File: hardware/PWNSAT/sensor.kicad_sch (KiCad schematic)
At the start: 15 parts, among them U1 ICM-42670-P, U2 SX1262IMLTRT, U4 BME280, U5 PE4259-63, Y3 CF4032M00010001

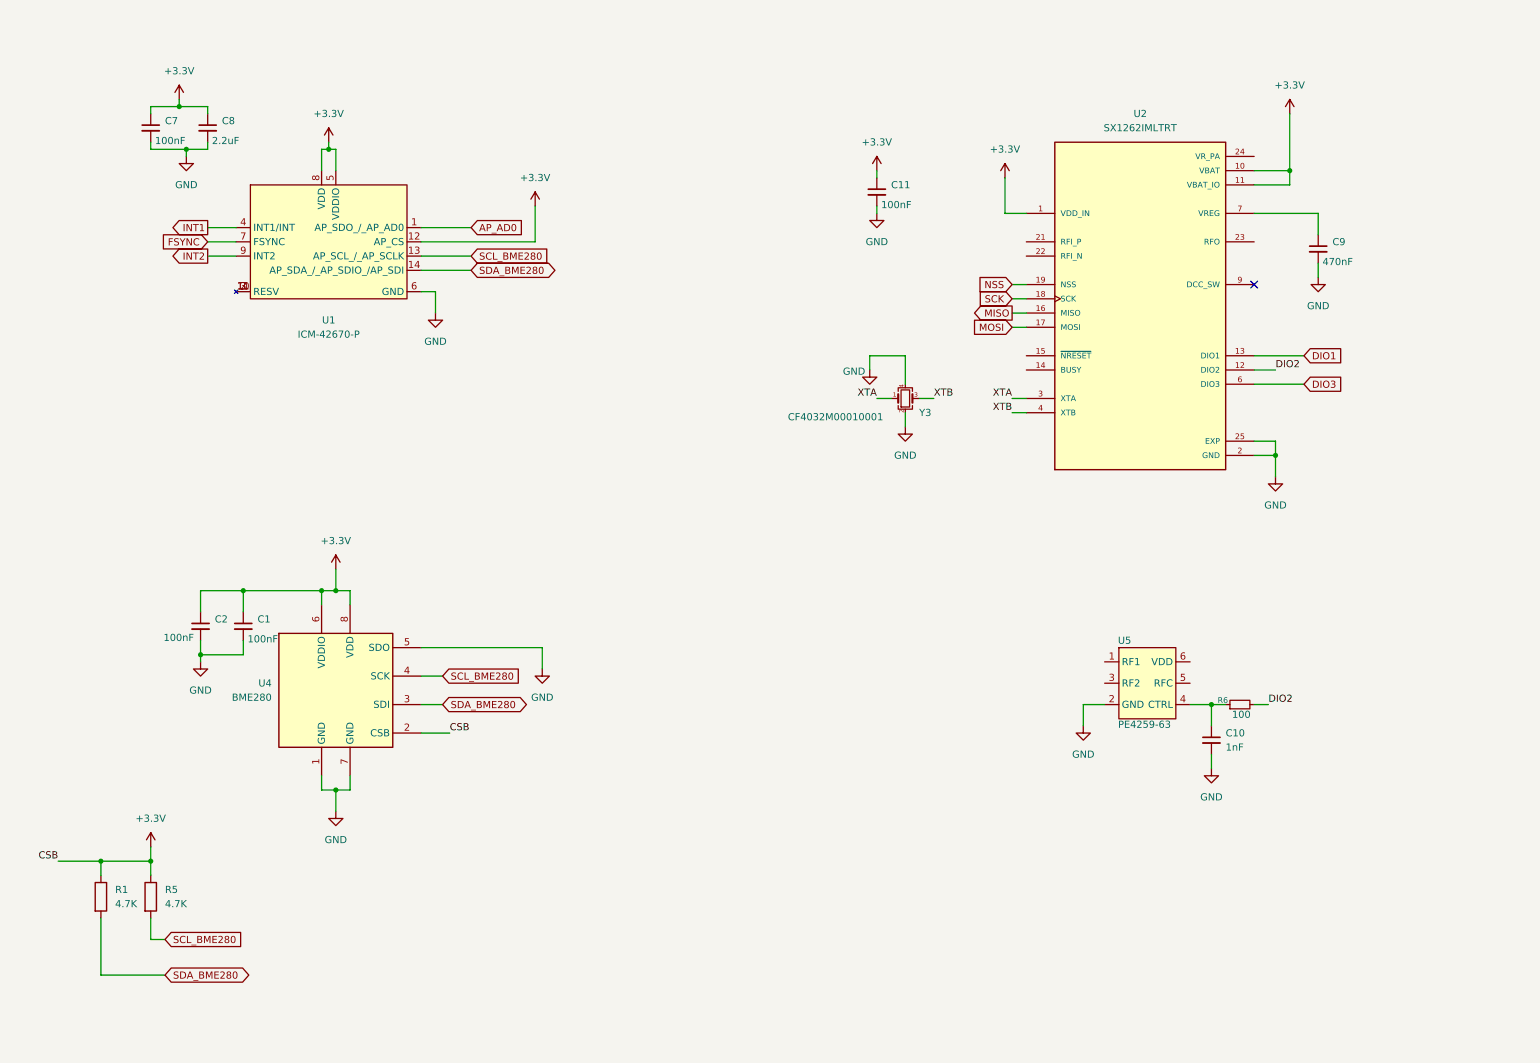
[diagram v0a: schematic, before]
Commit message: Feat(hw):Added_LoRa_module
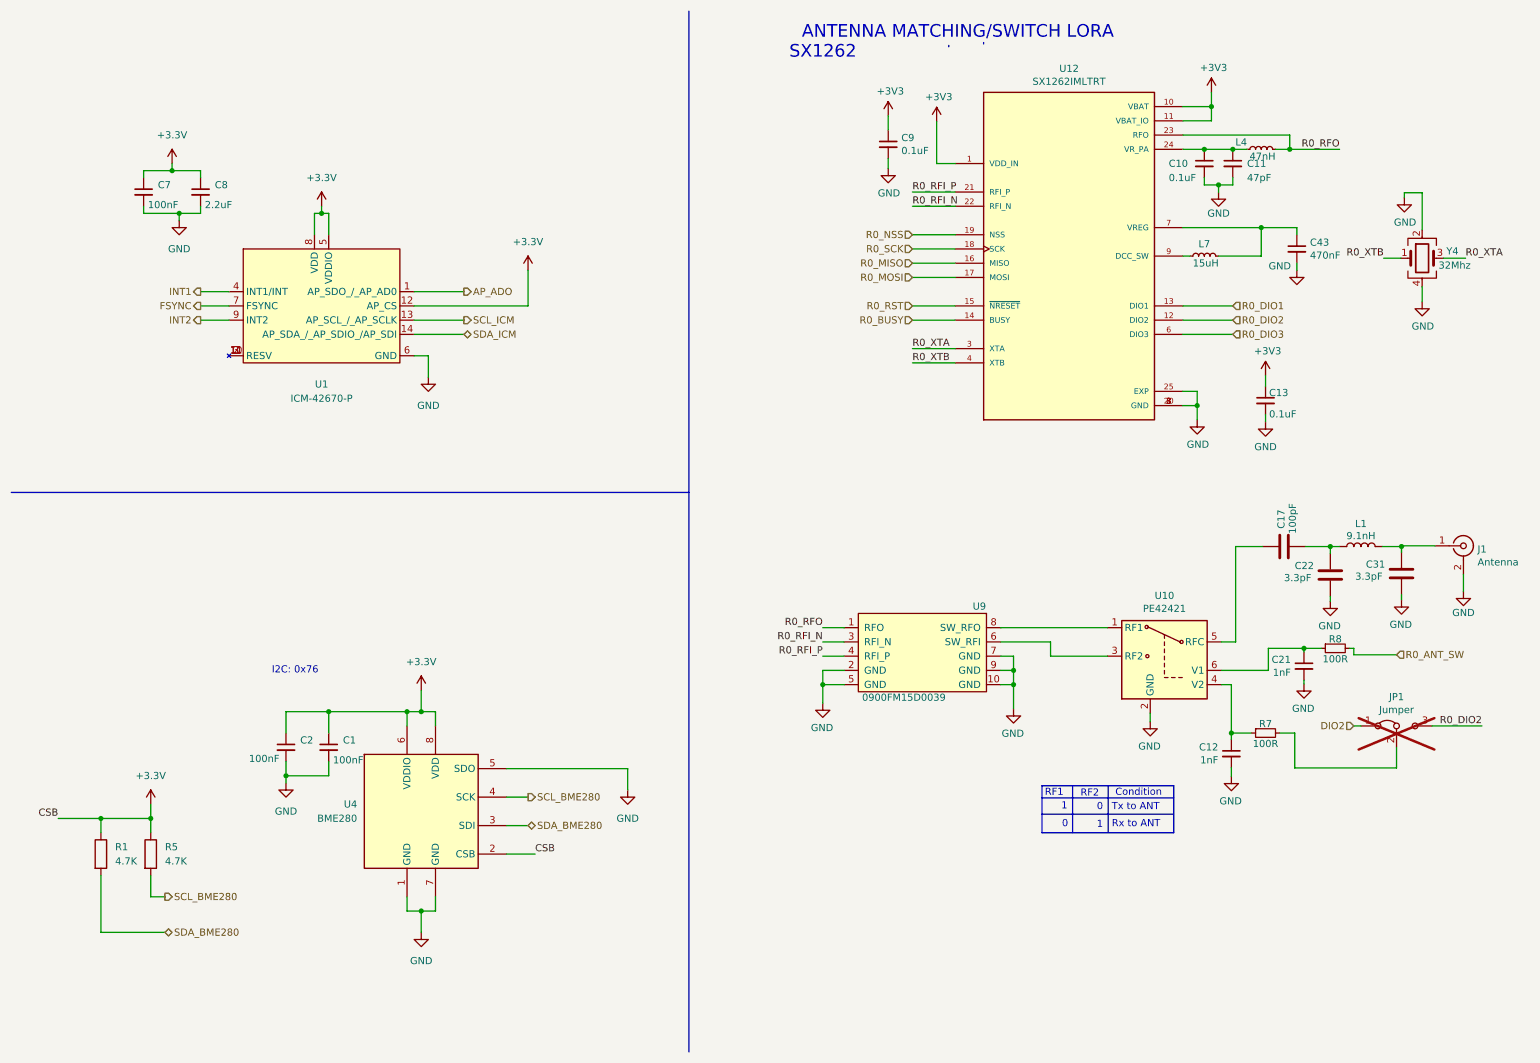
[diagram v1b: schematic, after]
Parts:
- removed C10: 1nF, symbol Device:C_Small
- removed C11: 100nF, symbol Device:C_Small
- removed C9: 470nF, symbol Device:C_Small
- removed R6: 100, symbol Device:R_Small
- removed U2: SX1262IMLTRT, SX1262IMLTRT:QFN50P400X400X100-25N, symbol SX1262IMLTRT:SX1262IMLTRT
- removed U5: PE4259-63, symbol Cubesat:PE4259-63
- removed Y3: CF4032M00010001, symbol Device:Crystal_GND24_Small
- added C10, C13, C9: 0.1uF, Capacitor_SMD:C_0402_1005Metric, symbol CatSniffer-rescue:C_Small-Device-CatStick-rescue-CatSniffer-rescue
- added C11: 47pF, Capacitor_SMD:C_0402_1005Metric, symbol CatSniffer-rescue:C_Small-Device-CatStick-rescue-CatSniffer-rescue
- added C12, C21: 1nF, Capacitor_SMD:C_0402_1005Metric, symbol CatSniffer-rescue:C_Small-Device-CatStick-rescue-CatSniffer-rescue
- added C17: 100pF, Capacitor_SMD:C_0402_1005Metric, symbol CatSniffer-rescue:C-Device-CatStick-rescue-CatSniffer-rescue
- added C22, C31: 3.3pF, Capacitor_SMD:C_0402_1005Metric, symbol CatSniffer-rescue:C-Device-CatStick-rescue-CatSniffer-rescue
- added C43: 470nF, Capacitor_SMD:C_0402_1005Metric, symbol CatSniffer-rescue:C_Small-Device-CatStick-rescue-CatSniffer-rescue
- added J1: Antenna, FlatSat:SMA_EDGE, symbol CatSniffer-rescue:Conn_Coaxial-Connector-CatStick-rescue-CatSniffer-rescue
- added JP1: Jumper, Jumper:SolderJumper-3_P1.3mm_Bridged12_RoundedPad1.0x1.5mm_NumberLabels, symbol CatSniffer-rescue:Jumper_3_Bridged12-Jumper-CatStick-rescue-CatSniffer-rescue
- added L1: 9.1nH, Inductor_SMD:L_0603_1608Metric, symbol CatSniffer-rescue:L-Device-CatStick-rescue-CatSniffer-rescue
- added L4: 47nH, Inductor_SMD:L_0603_1608Metric, symbol CatSniffer-rescue:L_Small-Device-CatStick-rescue-CatSniffer-rescue
- added L7: 15uH, Inductor_SMD:L_0603_1608Metric, symbol CatSniffer-rescue:L_Small-Device-CatStick-rescue-CatSniffer-rescue
- added R7, R8: 100R, Resistor_SMD:R_0402_1005Metric, symbol CatSniffer-rescue:R_Small-Device-CatStick-rescue-CatSniffer-rescue
- added U10: PE42421, Package_TO_SOT_SMD:SOT-363_SC-70-6, symbol CatSniffer-rescue:MASWSS0115-RF_Switch-CatStick-rescue-CatSniffer-rescue
- added U12: SX1262IMLTRT, Package_DFN_QFN:QFN-24-1EP_4x4mm_P0.5mm_EP2.65x2.65mm, symbol SX1262IMLTRT:SX1262IMLTRT
- added U9: 0900FM15D0039, FlatSat:0900FM15D0039E, symbol CatSniffer-rescue:0900FM15D0039-Electronic_Cats-CatStick-rescue-CatSniffer-resc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
- added Y4: 32Mhz, Crystal:Crystal_SMD_2520-4Pin_2.5x2.0mm, symbol CatSniffer-rescue:Crystal_GND24-Device-CatStick-rescue-CatSniffer-rescue
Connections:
- net DIO2: now also JP1.1 (A)
- net GND: now also C10.2, C11.2, C12.2, C13.2, C21.2, C22.2, C31.2, C43.2, C9.2, J1.2 (Ext), U10.2 (GND), U12.2 (GND), U12.20 (GND), U12.25 (EXP), U12.5 (GND), U12.8 (GND), U9.10 (GND), U9.2 (GND), U9.5 (GND), U9.7 (GND), U9.9 (GND), Y4.2, Y4.4
- net SCL_BME280: no longer U1.13 (AP_SCL_/_AP_SCLK)
- net SDA_BME280: no longer U1.14 (AP_SDA_/_AP_SDIO_/AP_SDI)
- net AP_AD0 renamed AP_ADO
- new net: C31.1, J1.1 (In), L1.1
- new net: C17.2, C22.1, L1.2
- new net: JP1.2 (C), R7.2
- new net: C12.1, R7.1, U10.4 (V2)
- new net: U10.1 (RF1), U9.8 (SW_RFO)
- new net: U10.3 (RF2), U9.6 (SW_RFI)
- new net: C17.1, U10.5 (RFC)
- new net: C21.1, R8.1, U10.6 (V1)
- new net: L7.1, U12.9 (DCC_SW)
- new net: C43.1, L7.2, U12.7 (VREG)
- new net: C10.1, C11.1, L4.1, U12.24 (VR_PA)
- new net +3V3: C13.1, C9.1, U12.1 (VDD_IN), U12.10 (VBAT), U12.11 (VBAT_IO)
- new net R0_ANT_SW: R8.2
- new net R0_BUSY: U12.14 (BUSY)
- new net R0_DIO1: U12.13 (DIO1)
- new net R0_DIO2: JP1.3 (B), U12.12 (DIO2)
- new net R0_DIO3: U12.6 (DIO3)
- new net R0_MISO: U12.16 (MISO)
- new net R0_MOSI: U12.17 (MOSI)
- new net R0_NSS: U12.19 (NSS)
- new net R0_RFI_N: U12.22 (RFI_N), U9.3 (RFI_N)
- new net R0_RFI_P: U12.21 (RFI_P), U9.4 (RFI_P)
- new net R0_RFO: L4.2, U12.23 (RFO), U9.1 (RFO)
- new net R0_RST: U12.15 (~{NRESET})
- new net R0_SCK: U12.18 (SCK)
- new net R0_XTA: U12.3 (XTA), Y4.3
- new net R0_XTB: U12.4 (XTB), Y4.1
- new net SCL_ICM: U1.13 (AP_SCL_/_AP_SCLK)
- new net SDA_ICM: U1.14 (AP_SDA_/_AP_SDIO_/AP_SDI)
- no-connect marks 1 -> 0
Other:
- note added: "0"
- note added: "1"
- note added: "ANTENNA MATCHING/SWITCH LORA"
- note added: "Condition"
- note added: "I2C: 0x76"
- note added: "RF1"
- note added: "RF2"
- note added: "Rx to ANT"
- note added: "SX1262"
- note added: "Tx to ANT"
- moved on the sheet: C1, C2, C7, C8, R1, R5, U1, U4

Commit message: feat(Hw): Added_BOM
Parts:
- C1, C2, C7: footprint (none) -> Capacitor_SMD:C_0402_1005Metric; #LCSC (none) -> C56392; LCSC# (none) -> C56392
- C10, C13, C9: #LCSC (none) -> C56392
- C11: #LCSC (none) -> C437519
- C12, C21: #LCSC (none) -> C710873
- C17: #LCSC (none) -> C541374
- C22, C31: #LCSC (none) -> C1565
- C43: #LCSC (none) -> C47339
- J1: #LCSC (none) -> C530661
- JP1: LCSC# (none) -> ---
- L1: #LCSC (none) -> C395094
- L4: #LCSC (none) -> C578001
- L7: #LCSC (none) -> C57838
- R1, R5: footprint (none) -> Resistor_SMD:R_0402_1005Metric_Pad0.72x0.64mm_HandSolder; #LCSC (none) -> C400631; LCSC# (none) -> C400631
- R7, R8: #LCSC (none) -> C25076
- U1: #LCSC (none) -> C3288646
- U10: #LCSC (none) -> C470893
- U12: #LCSC (none) -> C191341
- U4: #LCSC (none) -> C92489
- U9: MANUFACTURER (none) -> 0900FM15D0039E
- Y4: #LCSC (none) -> C255969
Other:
- note added: "ICM-42670-P"

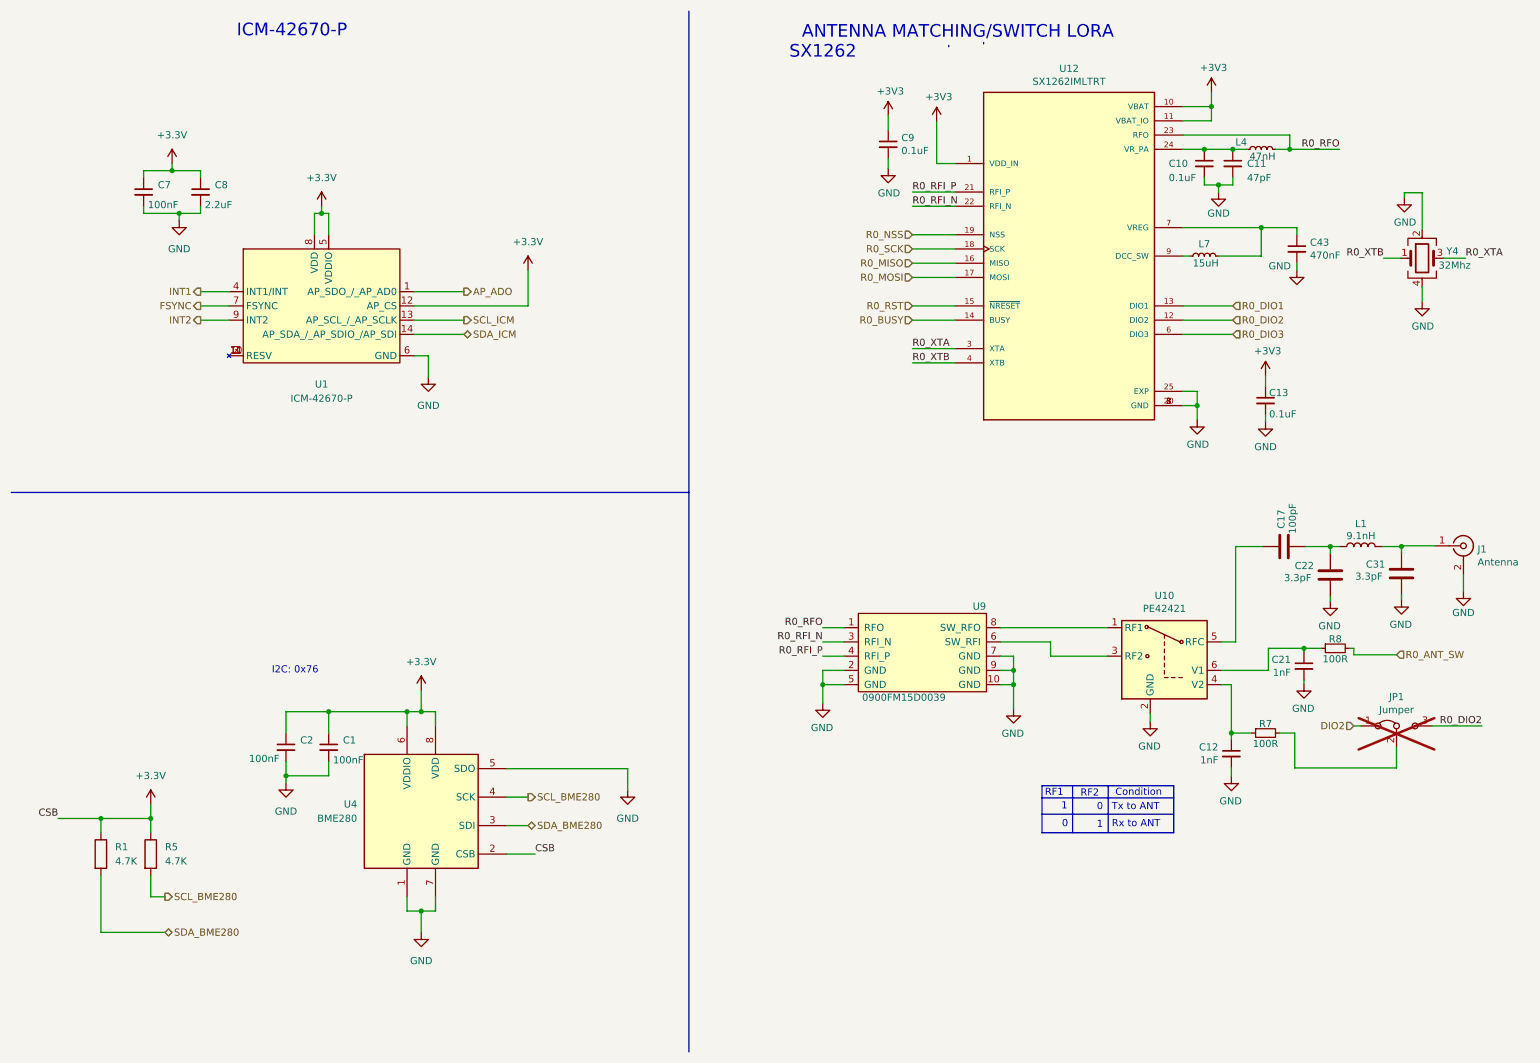
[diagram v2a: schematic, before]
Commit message: feat(Hw):Sch_Updated
Pending_Sensor_Connector
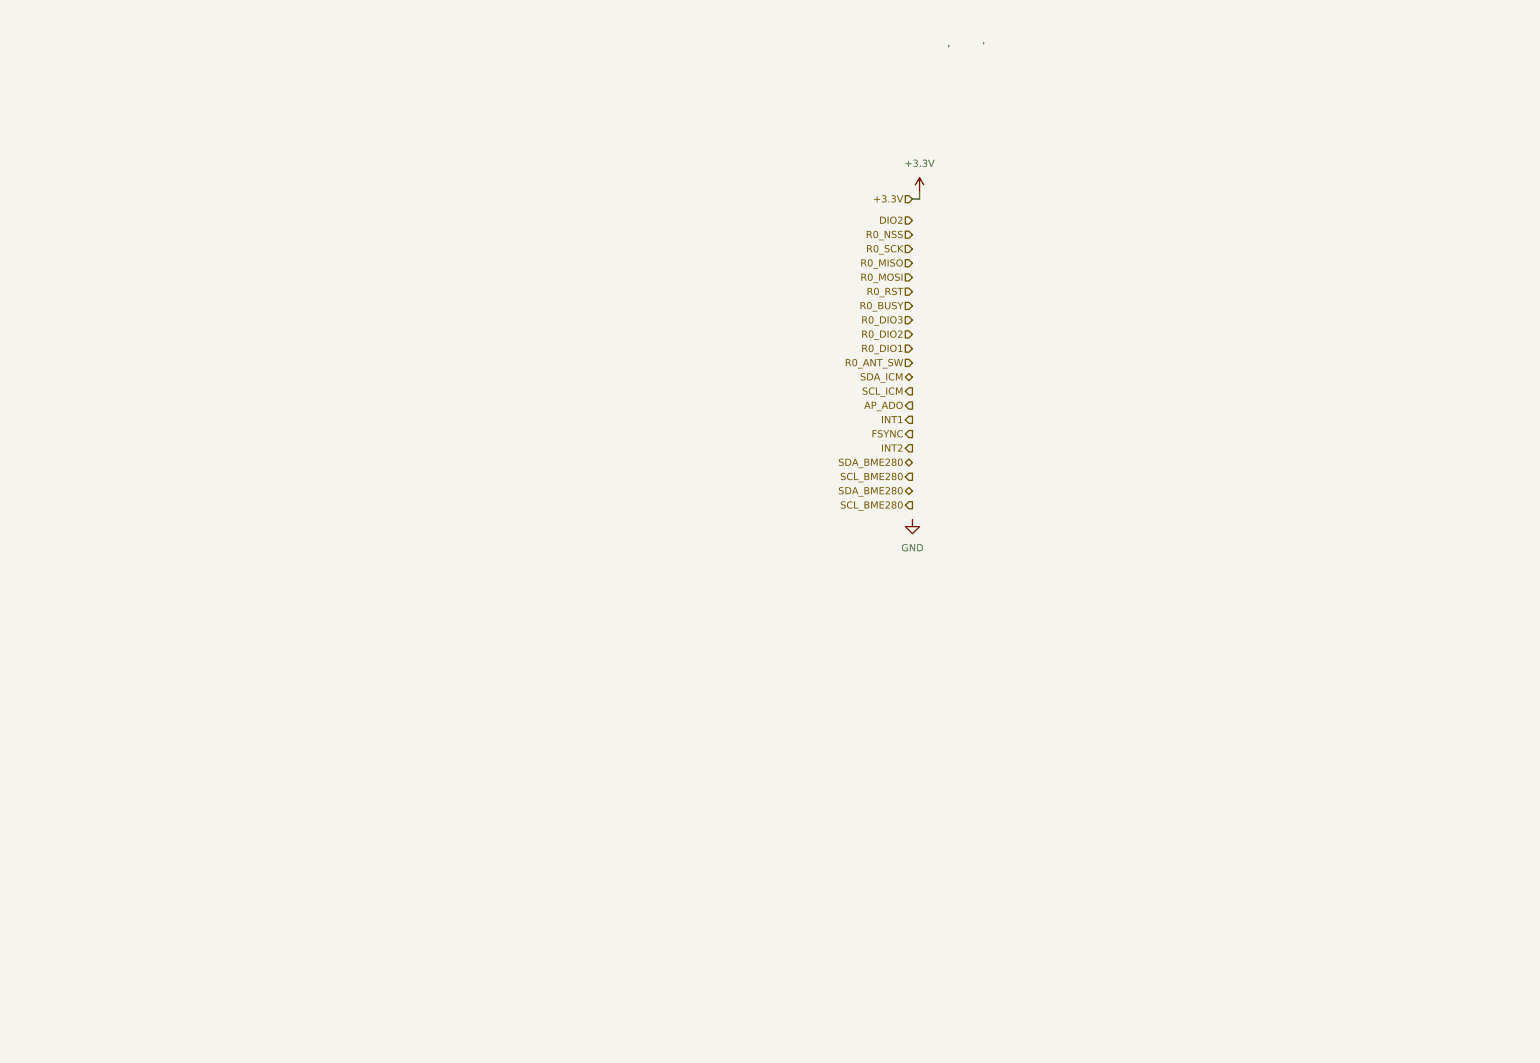
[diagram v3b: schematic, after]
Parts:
- removed C1, C2, C7: 100nF, Capacitor_SMD:C_0402_1005Metric, symbol Device:C_Small
- removed C10, C13, C9: 0.1uF, Capacitor_SMD:C_0402_1005Metric, symbol CatSniffer-rescue:C_Small-Device-CatStick-rescue-CatSniffer-rescue
- removed C11: 47pF, Capacitor_SMD:C_0402_1005Metric, symbol CatSniffer-rescue:C_Small-Device-CatStick-rescue-CatSniffer-rescue
- removed C12, C21: 1nF, Capacitor_SMD:C_0402_1005Metric, symbol CatSniffer-rescue:C_Small-Device-CatStick-rescue-CatSniffer-rescue
- removed C17: 100pF, Capacitor_SMD:C_0402_1005Metric, symbol CatSniffer-rescue:C-Device-CatStick-rescue-CatSniffer-rescue
- removed C22, C31: 3.3pF, Capacitor_SMD:C_0402_1005Metric, symbol CatSniffer-rescue:C-Device-CatStick-rescue-CatSniffer-rescue
- removed C43: 470nF, Capacitor_SMD:C_0402_1005Metric, symbol CatSniffer-rescue:C_Small-Device-CatStick-rescue-CatSniffer-rescue
- removed C8: 2.2uF, symbol Device:C_Small
- removed J1: Antenna, FlatSat:SMA_EDGE, symbol CatSniffer-rescue:Conn_Coaxial-Connector-CatStick-rescue-CatSniffer-rescue
- removed JP1: Jumper, Jumper:SolderJumper-3_P1.3mm_Bridged12_RoundedPad1.0x1.5mm_NumberLabels, symbol CatSniffer-rescue:Jumper_3_Bridged12-Jumper-CatStick-rescue-CatSniffer-rescue
- removed L1: 9.1nH, Inductor_SMD:L_0603_1608Metric, symbol CatSniffer-rescue:L-Device-CatStick-rescue-CatSniffer-rescue
- removed L4: 47nH, Inductor_SMD:L_0603_1608Metric, symbol CatSniffer-rescue:L_Small-Device-CatStick-rescue-CatSniffer-rescue
- removed L7: 15uH, Inductor_SMD:L_0603_1608Metric, symbol CatSniffer-rescue:L_Small-Device-CatStick-rescue-CatSniffer-rescue
- removed R1, R5: 4.7K, Resistor_SMD:R_0402_1005Metric_Pad0.72x0.64mm_HandSolder, symbol Device:R
- removed R7, R8: 100R, Resistor_SMD:R_0402_1005Metric, symbol CatSniffer-rescue:R_Small-Device-CatStick-rescue-CatSniffer-rescue
- removed U1: ICM-42670-P, symbol Cubesat:ICM-42670-P
- removed U10: PE42421, Package_TO_SOT_SMD:SOT-363_SC-70-6, symbol CatSniffer-rescue:MASWSS0115-RF_Switch-CatStick-rescue-CatSniffer-rescue
- removed U12: SX1262IMLTRT, Package_DFN_QFN:QFN-24-1EP_4x4mm_P0.5mm_EP2.65x2.65mm, symbol SX1262IMLTRT:SX1262IMLTRT
- removed U4: BME280, Package_LGA:Bosch_LGA-8_2.5x2.5mm_P0.65mm_ClockwisePinNumbering, symbol Sensor:BME280
- removed U9: 0900FM15D0039, FlatSat:0900FM15D0039E, symbol CatSniffer-rescue:0900FM15D0039-Electronic_Cats-CatStick-rescue-CatSniffer-resc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
- removed Y4: 32Mhz, Crystal:Crystal_SMD_2520-4Pin_2.5x2.0mm, symbol CatSniffer-rescue:Crystal_GND24-Device-CatStick-rescue-CatSniffer-rescue
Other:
- note removed: "0"
- note removed: "1"
- note removed: "ANTENNA MATCHING/SWITCH LORA"
- note removed: "Condition"
- note removed: "I2C: 0x76"
- note removed: "ICM-42670-P"
- note removed: "RF1"
- note removed: "RF2"
- note removed: "Rx to ANT"
- note removed: "SX1262"
- note removed: "Tx to ANT"
